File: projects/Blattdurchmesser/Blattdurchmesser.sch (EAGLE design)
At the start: 15 parts, among them K1 TX2_RELAY", Q1 ARDUINOR3-NOIOREF-NOTEXT

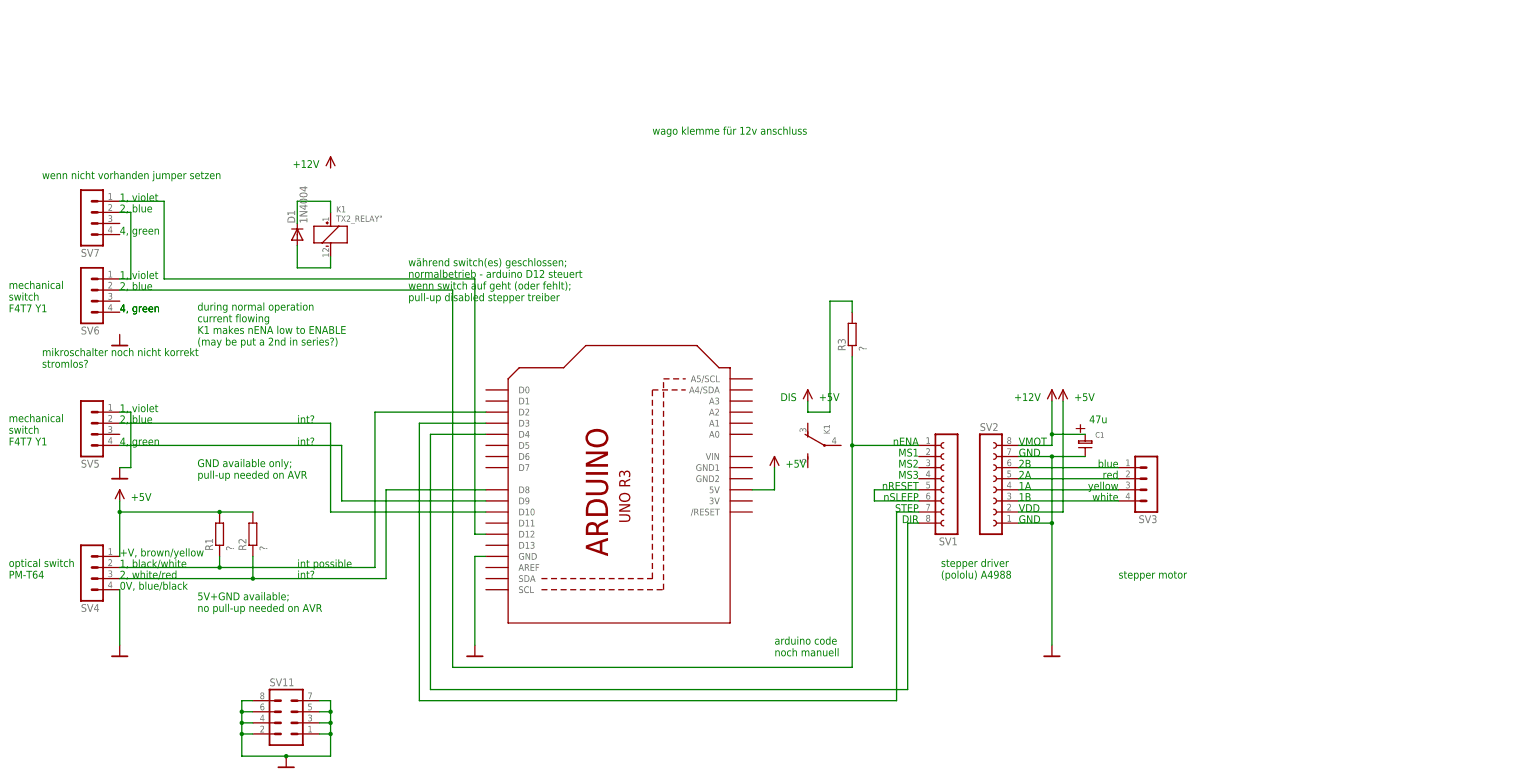
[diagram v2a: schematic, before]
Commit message: improvement; * put everything closer to meet space restrictions              * add 7805 (+5V) voltage regulator (derive from +12V)              * add a wire clamp for +12V power connection
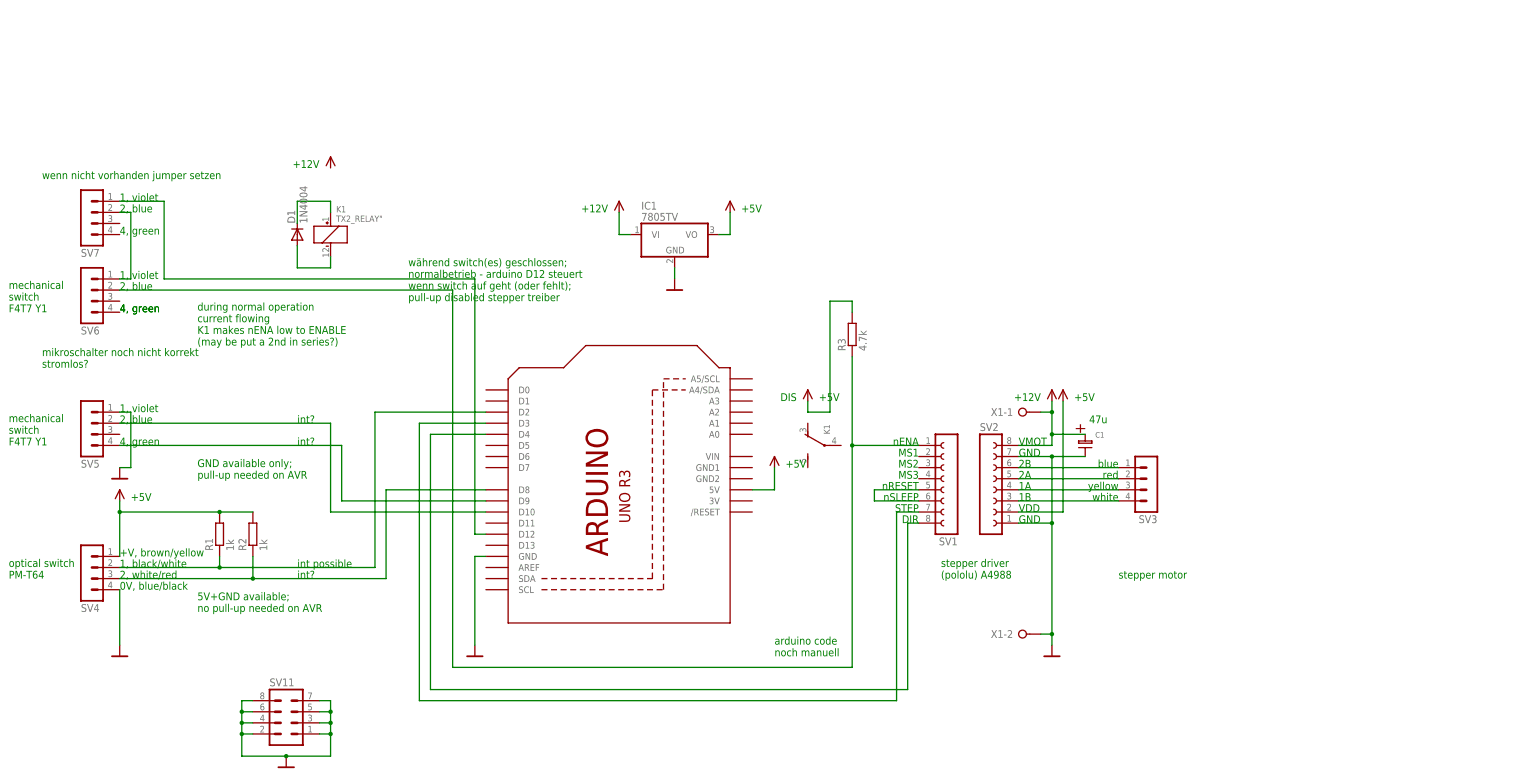
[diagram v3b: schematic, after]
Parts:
- added IC1: 7805TV, linear:7805TV
- added X1: (no value), con-wago-508:W237-02P
- R1, R2: value ? -> 1k
- R3: value ? -> 4.7k
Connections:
- net +12V: now also IC1.VI, X1-1.KL
- net +5V: now also IC1.VO
- net GND: now also IC1.GND, X1-2.KL
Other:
- note removed: "wago klemme für 12v anschluss"
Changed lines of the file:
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@@
 <part name="C1" library="Elkos" deviceset="R_ELKO_8.1" device=""/>
 <part name="SV5" library="con-lstb" deviceset="MA04-1" device=""/>
-<part name="R1" library="rcl" deviceset="R-EU_" device="0207/10" value="?"/>
-<part name="R2" library="rcl" deviceset="R-EU_" device="0207/10" value="?"/>
+<part name="R1" library="rcl" deviceset="R-EU_" device="0207/10" value="1k"/>
+<part name="R2" library="rcl" deviceset="R-EU_" device="0207/10" value="1k"/>
 <part name="U$9" library="Netze" deviceset="+5V" device=""/>
 <part name="U$10" library="Netze" deviceset="GND" device=""/>
@@
 <part name="U$13" library="Netze" deviceset="+12V" device=""/>
 <part name="D1" library="diode" deviceset="1N4004" device=""/>
-<part name="R3" library="rcl" deviceset="R-EU_" device="0207/10" value="?"/>
+<part name="R3" library="rcl" deviceset="R-EU_" device="0207/10" value="4.7k"/>
 <part name="Q1" library="adafruit" deviceset="ARDUINOR3-NOIOREF" device="-NOTEXT"/>
 <part name="SV7" library="con-lstb" deviceset="MA04-1" device=""/>
+<part name="X1" library="con-wago-508" deviceset="W237-02P" device=""/>
+<part name="IC1" library="linear" deviceset="78*" device="TV" technology="05"/>
+<part name="U$2" library="Netze" deviceset="+12V" device=""/>
+<part name="U$14" library="Netze" deviceset="+5V" device=""/>
 </parts>
 <sheets>
@@
 <text x="-30.48" y="76.2" size="1.778" layer="91">4, green</text>
 <text x="-30.48" y="93.98" size="1.778" layer="91">4, green</text>
-<text x="91.44" y="116.84" size="1.778" layer="91">wago klemme für 12v anschluss</text>
+<text x="81.28" y="99.06" size="1.778" layer="91" align="bottom-right">+12V</text>
+<text x="111.76" y="99.06" size="1.778" layer="91">+5V</text>
 </plain>
 <instances>
@@
 <instance part="U$11" gate="1" x="7.62" y="-25.4"/>
 <instance part="SV6" gate="1" x="-38.1" y="78.74" rot="MR180"/>
-<instance part="U$12" gate="1" x="-30.48" y="71.12"/>
+<instance part="U$12" gate="1" x="96.52" y="83.82"/>
 <instance part="U$13" gate="1" x="17.78" y="104.14"/>
 <instance part="D1" gate="1" x="10.16" y="93.98" rot="R90"/>
@@
 <instance part="Q1" gate="G$1" x="83.82" y="38.1" rot="R90"/>
 <instance part="SV7" gate="1" x="-38.1" y="96.52" rot="MR180"/>
+<instance part="X1" gate="-1" x="175.26" y="53.34"/>
+<instance part="X1" gate="-2" x="175.26" y="2.54"/>
+<instance part="IC1" gate="A1" x="96.52" y="93.98"/>
+<instance part="U$2" gate="1" x="83.82" y="93.98"/>
+<instance part="U$14" gate="1" x="109.22" y="99.06"/>
 </instances>
 <busses>
@@
 <segment>
 <pinref part="U$1" gate="1" pin="GND"/>
-<wire x1="182.88" y1="0" x2="182.88" y2="27.94" width="0.1524" layer="91"/>
+<wire x1="182.88" y1="0" x2="182.88" y2="2.54" width="0.1524" layer="91"/>
 <pinref part="SV2" gate="G$1" pin="1"/>
+<wire x1="182.88" y1="2.54" x2="182.88" y2="27.94" width="0.1524" layer="91"/>
 <wire x1="182.88" y1="27.94" x2="175.26" y2="27.94" width="0.1524" layer="91"/>
 <pinref part="SV2" gate="G$1" pin="7"/>
@@
 <wire x1="182.88" y1="43.18" x2="190.5" y2="43.18" width="0.1524" layer="91"/>
 <junction x="182.88" y="43.18"/>
+<pinref part="X1" gate="-2" pin="KL"/>
+<wire x1="180.34" y1="2.54" x2="182.88" y2="2.54" width="0.1524" layer="91"/>
+<junction x="182.88" y="2.54"/>
 </segment>
 <segment>
@@
 <junction x="7.62" y="-25.4"/>
 </segment>
+<segment>
+<pinref part="IC1" gate="A1" pin="GND"/>
+<pinref part="U$12" gate="1" pin="GND"/>
+<wire x1="96.52" y1="86.36" x2="96.52" y2="83.82" width="0.1524" layer="91"/>
+</segment>
 </net>
 <net name="+5V" class="0">
@@
 <wire x1="137.16" y1="78.74" x2="137.16" y2="76.2" width="0.1524" layer="91"/>
 </segment>
+<segment>
+<pinref part="IC1" gate="A1" pin="VO"/>
+<pinref part="U$14" gate="1" pin="+5V"/>
+<wire x1="106.68" y1="93.98" x2="109.22" y2="93.98" width="0.1524" layer="91"/>
+<wire x1="109.22" y1="93.98" x2="109.22" y2="99.06" width="0.1524" layer="91"/>
+</segment>
 </net>
 <net name="+12V" class="0">
@@
 <pinref part="U$6" gate="1" pin="+12V"/>
 <pinref part="C1" gate="G$1" pin="P"/>
-<wire x1="182.88" y1="48.26" x2="182.88" y2="55.88" width="0.1524" layer="91"/>
+<wire x1="182.88" y1="48.26" x2="182.88" y2="53.34" width="0.1524" layer="91"/>
+<wire x1="182.88" y1="53.34" x2="182.88" y2="55.88" width="0.1524" layer="91"/>
 <wire x1="190.5" y1="48.26" x2="182.88" y2="48.26" width="0.1524" layer="91"/>
 <junction x="182.88" y="48.26"/>
+<pinref part="X1" gate="-1" pin="KL"/>
+<wire x1="180.34" y1="53.34" x2="182.88" y2="53.34" width="0.1524" layer="91"/>
+<junction x="182.88" y="53.34"/>
+</segment>
+<segment>
+<pinref part="U$2" gate="1" pin="+12V"/>
+<wire x1="83.82" y1="99.06" x2="83.82" y2="93.98" width="0.1524" layer="91"/>
+<pinref part="IC1" gate="A1" pin="VI"/>
+<wire x1="83.82" y1="93.98" x2="86.36" y2="93.98" width="0.1524" layer="91"/>
 </segment>
 </net>
@@
 </sheet>
 </sheets>
-<errors>
-</errors>
 </schematic>
 </drawing>

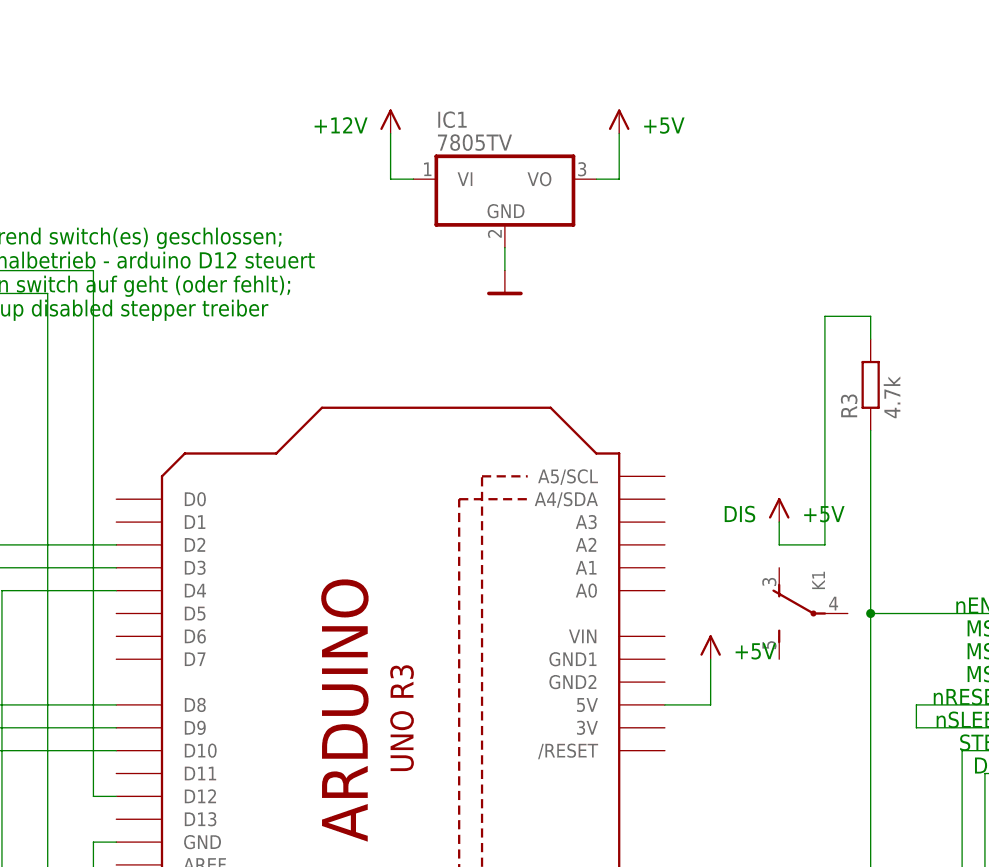
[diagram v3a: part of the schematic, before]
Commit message: improvement; * replace 7805 voltage regulator by Arduino on-board one
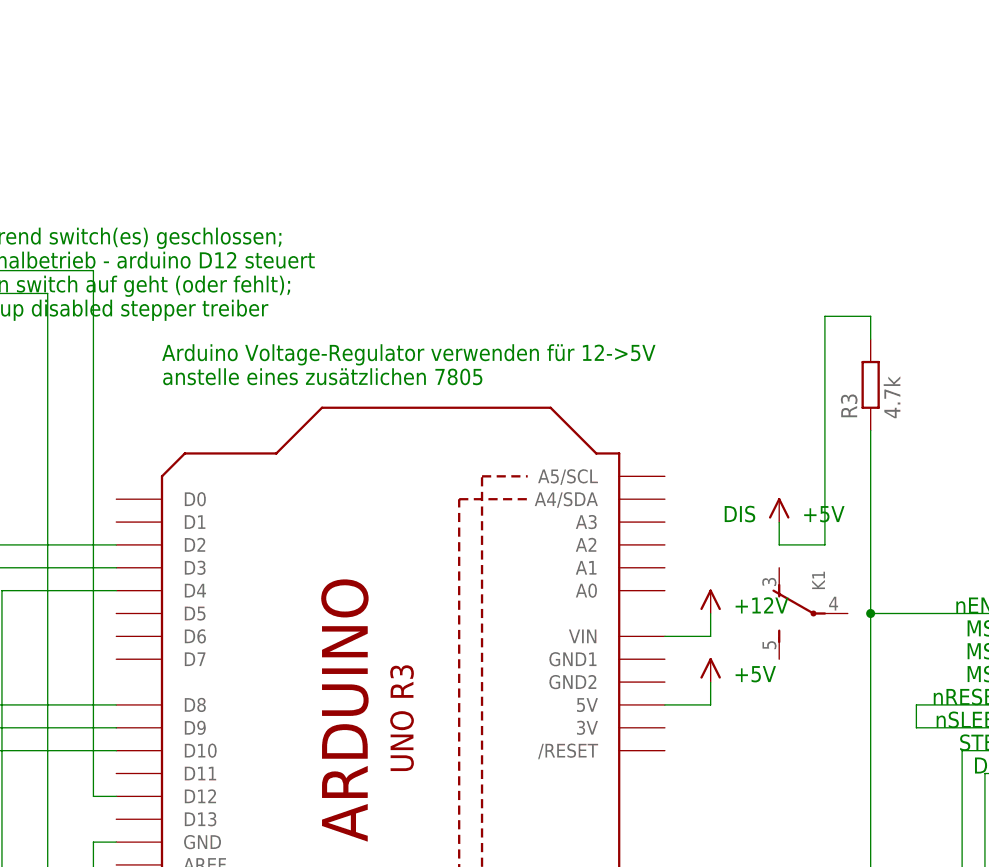
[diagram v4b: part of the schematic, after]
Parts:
- removed IC1: 7805TV, linear:7805TV
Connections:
- net +12V: now also Q1.VIN; no longer IC1.VI
- net +5V: no longer IC1.VO
- net GND: no longer IC1.GND
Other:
- note added: "Arduino Voltage-Regulator verwenden für 12->5V anstelle eines zusätzlichen 7805"
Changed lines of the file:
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@@
 <part name="U$11" library="Netze" deviceset="GND" device=""/>
 <part name="SV6" library="con-lstb" deviceset="MA04-1" device=""/>
-<part name="U$12" library="Netze" deviceset="GND" device=""/>
 <part name="U$13" library="Netze" deviceset="+12V" device=""/>
 <part name="D1" library="diode" deviceset="1N4004" device=""/>
@@
 <part name="SV7" library="con-lstb" deviceset="MA04-1" device=""/>
 <part name="X1" library="con-wago-508" deviceset="W237-02P" device=""/>
-<part name="IC1" library="linear" deviceset="78*" device="TV" technology="05"/>
 <part name="U$2" library="Netze" deviceset="+12V" device=""/>
-<part name="U$14" library="Netze" deviceset="+5V" device=""/>
 </parts>
 <sheets>
@@
 <text x="198.12" y="35.56" size="1.778" layer="91" align="bottom-right">yellow</text>
 <text x="198.12" y="33.02" size="1.778" layer="91" align="bottom-right">white</text>
-<text x="121.92" y="40.64" size="1.778" layer="91">+5V</text>
+<text x="121.92" y="38.1" size="1.778" layer="91">+5V</text>
 <text x="129.54" y="55.88" size="1.778" layer="91">+5V</text>
 <text x="124.46" y="55.88" size="1.778" layer="91" align="bottom-right">DIS</text>
@@
 <text x="-30.48" y="76.2" size="1.778" layer="91">4, green</text>
 <text x="-30.48" y="93.98" size="1.778" layer="91">4, green</text>
-<text x="81.28" y="99.06" size="1.778" layer="91" align="bottom-right">+12V</text>
-<text x="111.76" y="99.06" size="1.778" layer="91">+5V</text>
+<text x="121.92" y="45.72" size="1.778" layer="91">+12V</text>
+<text x="58.42" y="71.12" size="1.778" layer="91">Arduino Voltage-Regulator verwenden für 12-&gt;5V
+anstelle eines zusätzlichen 7805</text>
 </plain>
 <instances>
@@
 <instance part="U$6" gate="1" x="182.88" y="50.8"/>
 <instance part="SV3" gate="1" x="205.74" y="35.56" rot="R180"/>
-<instance part="U$7" gate="1" x="119.38" y="40.64"/>
+<instance part="U$7" gate="1" x="119.38" y="38.1"/>
 <instance part="U$8" gate="1" x="127" y="55.88"/>
 <instance part="C1" gate="G$1" x="190.5" y="45.72"/>
@@
 <instance part="U$11" gate="1" x="7.62" y="-25.4"/>
 <instance part="SV6" gate="1" x="-38.1" y="78.74" rot="MR180"/>
-<instance part="U$12" gate="1" x="96.52" y="83.82"/>
 <instance part="U$13" gate="1" x="17.78" y="104.14"/>
 <instance part="D1" gate="1" x="10.16" y="93.98" rot="R90"/>
@@
 <instance part="X1" gate="-1" x="175.26" y="53.34"/>
 <instance part="X1" gate="-2" x="175.26" y="2.54"/>
-<instance part="IC1" gate="A1" x="96.52" y="93.98"/>
-<instance part="U$2" gate="1" x="83.82" y="93.98"/>
-<instance part="U$14" gate="1" x="109.22" y="99.06"/>
+<instance part="U$2" gate="1" x="119.38" y="40.64"/>
 </instances>
 <busses>
@@
 <junction x="7.62" y="-25.4"/>
 </segment>
-<segment>
-<pinref part="IC1" gate="A1" pin="GND"/>
-<pinref part="U$12" gate="1" pin="GND"/>
-<wire x1="96.52" y1="86.36" x2="96.52" y2="83.82" width="0.1524" layer="91"/>
-</segment>
 </net>
 <net name="+5V" class="0">
@@
 <segment>
 <pinref part="U$7" gate="1" pin="+5V"/>
-<wire x1="119.38" y1="35.56" x2="119.38" y2="40.64" width="0.1524" layer="91"/>
+<wire x1="119.38" y1="35.56" x2="119.38" y2="38.1" width="0.1524" layer="91"/>
 <pinref part="Q1" gate="G$1" pin="5V"/>
 <wire x1="119.38" y1="35.56" x2="114.3" y2="35.56" width="0.1524" layer="91"/>
@@
 <wire x1="132.08" y1="78.74" x2="137.16" y2="78.74" width="0.1524" layer="91"/>
 <wire x1="137.16" y1="78.74" x2="137.16" y2="76.2" width="0.1524" layer="91"/>
-</segment>
-<segment>
-<pinref part="IC1" gate="A1" pin="VO"/>
-<pinref part="U$14" gate="1" pin="+5V"/>
-<wire x1="106.68" y1="93.98" x2="109.22" y2="93.98" width="0.1524" layer="91"/>
-<wire x1="109.22" y1="93.98" x2="109.22" y2="99.06" width="0.1524" layer="91"/>
 </segment>
 </net>
@@
 <segment>
 <pinref part="U$2" gate="1" pin="+12V"/>
-<wire x1="83.82" y1="99.06" x2="83.82" y2="93.98" width="0.1524" layer="91"/>
-<pinref part="IC1" gate="A1" pin="VI"/>
-<wire x1="83.82" y1="93.98" x2="86.36" y2="93.98" width="0.1524" layer="91"/>
+<wire x1="119.38" y1="45.72" x2="119.38" y2="43.18" width="0.1524" layer="91"/>
+<pinref part="Q1" gate="G$1" pin="VIN"/>
+<wire x1="119.38" y1="43.18" x2="114.3" y2="43.18" width="0.1524" layer="91"/>
 </segment>
 </net>
